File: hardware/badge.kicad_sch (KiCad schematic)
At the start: 2 parts

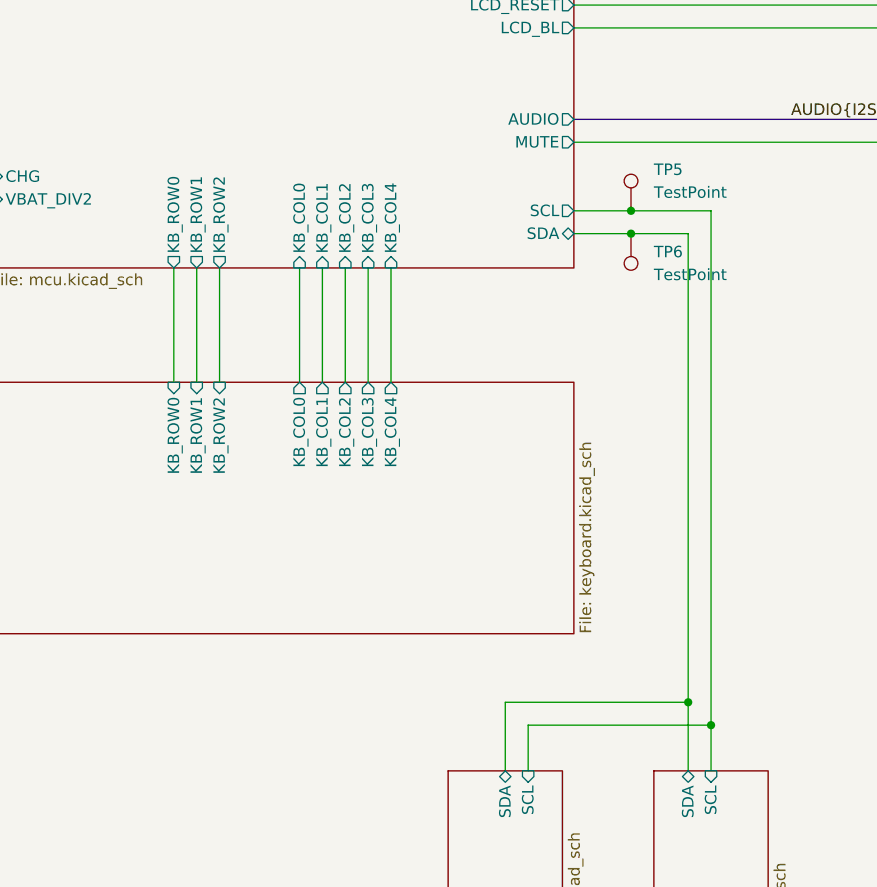
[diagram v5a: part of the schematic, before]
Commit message: remove mux, use i2c expander for keyboard
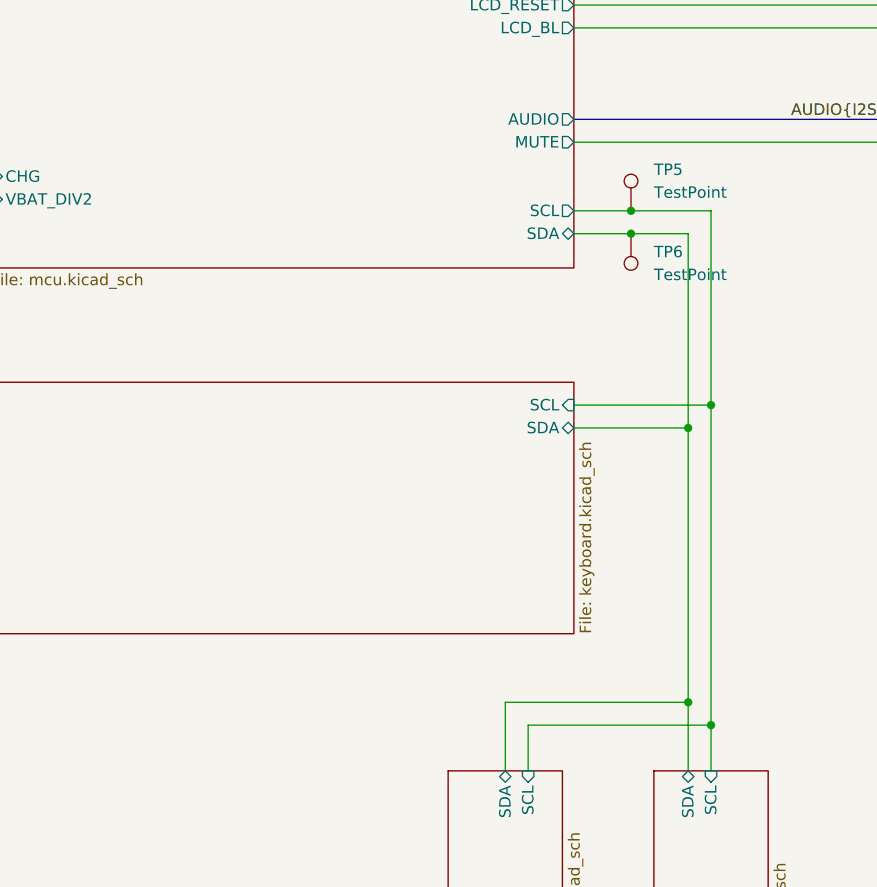
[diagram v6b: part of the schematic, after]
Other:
- sheet keyboard ports: added SCL, SDA; removed KB_COL0, KB_COL1, KB_COL2, KB_COL3, KB_COL4, KB_ROW0, KB_ROW1, KB_ROW2
- sheet mcu ports: added none; removed KB_COL0, KB_COL1, KB_COL2, KB_COL3, KB_COL4, KB_ROW0, KB_ROW1, KB_ROW2
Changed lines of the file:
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@@
+	)
+	(junction
+		(at 146.05 91.44)
+		(diameter 0)
+		(color 0 0 0 0)
 	)
 	(junction
@@
 		(color 0 0 0 0)
 	)
+	(junction
+		(at 148.59 88.9)
+		(diameter 0)
+		(color 0 0 0 0)
+	)
 	(no_connect
 		(at 196.85 49.53)
@@
 	(wire
 		(pts
-			(xy 91.44 73.66) (xy 91.44 86.36)
-		)
-		(stroke
-			(width 0)
-			(type default)
-		)
-	)
-	(wire
-		(pts
-			(xy 93.98 73.66) (xy 93.98 86.36)
-		)
-		(stroke
-			(width 0)
-			(type default)
-		)
-	)
-	(wire
-		(pts
 			(xy 133.35 44.45) (xy 196.85 44.45)
 		)
@@
 		)
 	)
-	(wire
-		(pts
-			(xy 113.03 73.66) (xy 113.03 86.36)
-		)
-		(stroke
-			(width 0)
-			(type default)
-		)
-	)
 	(bus
 		(pts
@@
 	(wire
 		(pts
-			(xy 146.05 69.85) (xy 146.05 121.92)
+			(xy 146.05 69.85) (xy 146.05 91.44)
 		)
 		(stroke
@@
 	(wire
 		(pts
-			(xy 148.59 67.31) (xy 148.59 124.46)
-		)
-		(stroke
-			(width 0)
-			(type default)
-		)
-	)
-	(wire
-		(pts
-			(xy 88.9 73.66) (xy 88.9 86.36)
+			(xy 148.59 67.31) (xy 148.59 88.9)
 		)
 		(stroke
@@
 		)
 	)
-	(wire
-		(pts
-			(xy 110.49 73.66) (xy 110.49 86.36)
-		)
-		(stroke
-			(width 0)
-			(type default)
-		)
-	)
 	(bus
 		(pts
@@
 	(wire
 		(pts
-			(xy 105.41 73.66) (xy 105.41 86.36)
-		)
-		(stroke
-			(width 0)
-			(type default)
-		)
-	)
-	(wire
-		(pts
 			(xy 58.42 36.83) (xy 68.58 36.83)
 		)
@@
 	(wire
 		(pts
+			(xy 146.05 91.44) (xy 146.05 121.92)
+		)
+		(stroke
+			(width 0)
+			(type default)
+		)
+	)
+	(wire
+		(pts
 			(xy 58.42 40.64) (xy 68.58 40.64)
 		)
@@
 	(wire
 		(pts
+			(xy 133.35 88.9) (xy 148.59 88.9)
+		)
+		(stroke
+			(width 0)
+			(type default)
+		)
+	)
+	(wire
+		(pts
 			(xy 139.7 67.31) (xy 148.59 67.31)
 		)
@@
 	(wire
 		(pts
-			(xy 107.95 73.66) (xy 107.95 86.36)
-		)
-		(stroke
-			(width 0)
-			(type default)
-		)
-	)
-	(wire
-		(pts
 			(xy 133.35 36.83) (xy 196.85 36.83)
 		)
@@
 	(wire
 		(pts
+			(xy 133.35 91.44) (xy 146.05 91.44)
+		)
+		(stroke
+			(width 0)
+			(type default)
+		)
+	)
+	(wire
+		(pts
 			(xy 148.59 124.46) (xy 148.59 129.54)
 		)
@@
 	(wire
 		(pts
-			(xy 102.87 73.66) (xy 102.87 86.36)
-		)
-		(stroke
-			(width 0)
-			(type default)
-		)
-	)
-	(wire
-		(pts
 			(xy 133.35 59.69) (xy 167.64 59.69)
+		)
+		(stroke
+			(width 0)
+			(type default)
+		)
+	)
+	(wire
+		(pts
+			(xy 148.59 88.9) (xy 148.59 124.46)
 		)
 		(stroke
@@
 			)
 		)
-		(pin "KB_ROW0" input
-			(at 88.9 86.36 90)
-			(effects
-				(font
-					(size 1.27 1.27)
-				)
-				(justify right)
-			)
-		)
-		(pin "KB_ROW1" input
-			(at 91.44 86.36 90)
-			(effects
-				(font
-					(size 1.27 1.27)
-				)
-				(justify right)
-			)
-		)
-		(pin "KB_ROW2" input
-			(at 93.98 86.36 90)
-			(effects
-				(font
-					(size 1.27 1.27)
-				)
-				(justify right)
-			)
-		)
-		(pin "KB_COL4" output
-			(at 113.03 86.36 90)
-			(effects
-				(font
-					(size 1.27 1.27)
-				)
-				(justify right)
-			)
-		)
-		(pin "KB_COL2" output
-			(at 107.95 86.36 90)
-			(effects
-				(font
-					(size 1.27 1.27)
-				)
-				(justify right)
-			)
-		)
-		(pin "KB_COL3" output
-			(at 110.49 86.36 90)
-			(effects
-				(font
-					(size 1.27 1.27)
-				)
-				(justify right)
-			)
-		)
-		(pin "KB_COL0" output
-			(at 102.87 86.36 90)
-			(effects
-				(font
-					(size 1.27 1.27)
-				)
-				(justify right)
-			)
-		)
-		(pin "KB_COL1" output
-			(at 105.41 86.36 90)
+		(pin "SCL" input
+			(at 133.35 88.9 0)
+			(effects
+				(font
+					(size 1.27 1.27)
+				)
+				(justify right)
+			)
+		)
+		(pin "SDA" bidirectional
+			(at 133.35 91.44 0)
 			(effects
 				(font
@@
 			)
 		)
-		(pin "KB_COL0" input
-			(at 102.87 73.66 270)
-			(effects
-				(font
-					(size 1.27 1.27)
-				)
-				(justify left)
-			)
-		)
-		(pin "KB_COL2" input
-			(at 107.95 73.66 270)
-			(effects
-				(font
-					(size 1.27 1.27)
-				)
-				(justify left)
-			)
-		)
-		(pin "KB_COL3" input
-			(at 110.49 73.66 270)
-			(effects
-				(font
-					(size 1.27 1.27)
-				)
-				(justify left)
-			)
-		)
-		(pin "KB_COL4" input
-			(at 113.03 73.66 270)
-			(effects
-				(font
-					(size 1.27 1.27)
-				)
-				(justify left)
-			)
-		)
-		(pin "KB_COL1" input
-			(at 105.41 73.66 270)
-			(effects
-				(font
-					(size 1.27 1.27)
-				)
-				(justify left)
-			)
-		)
 		(pin "CHG" input
 			(at 68.58 63.5 180)
@@
 			(effects
 				(font
-					(size 1.27 1.27)
-				)
-				(justify left)
-			)
-		)
-		(pin "KB_ROW0" output
-			(at 88.9 73.66 270)
-			(effects
-				(font
-					(size 1.27 1.27)
-				)
-				(justify left)
-			)
-		)
-		(pin "KB_ROW1" output
-			(at 91.44 73.66 270)
-			(effects
-				(font
-					(size 1.27 1.27)
-				)
-				(justify left)
-			)
-		)
-		(pin "KB_ROW2" output
-			(at 93.98 73.66 270)
-			(effects
-				(font

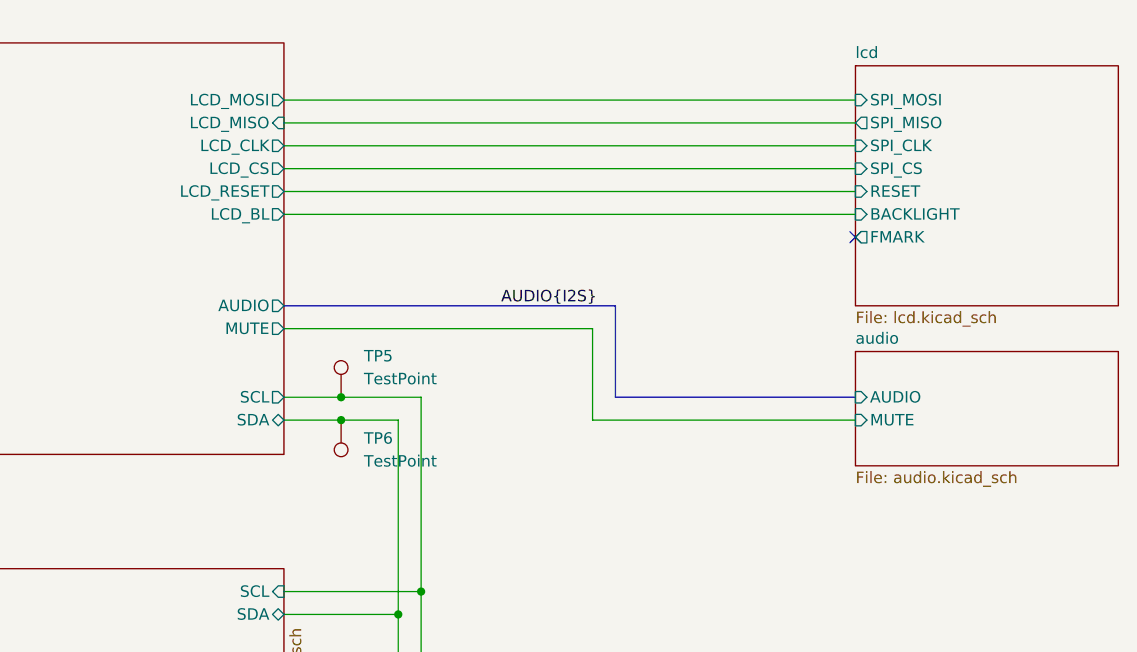
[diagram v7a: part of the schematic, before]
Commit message: Create a preliminary routing
Disconnect the LORA module from the lcd bus
Add netclass and lenght matching rule for the LCD signals
Use Bus for spi syglas for easy netclass association
Remove cutaway jumper for the io expansions, and hardcode the address
Routed the keyboard matrix
Change the LCD resistor to 1202
Fix the0Ohm resistor footprint
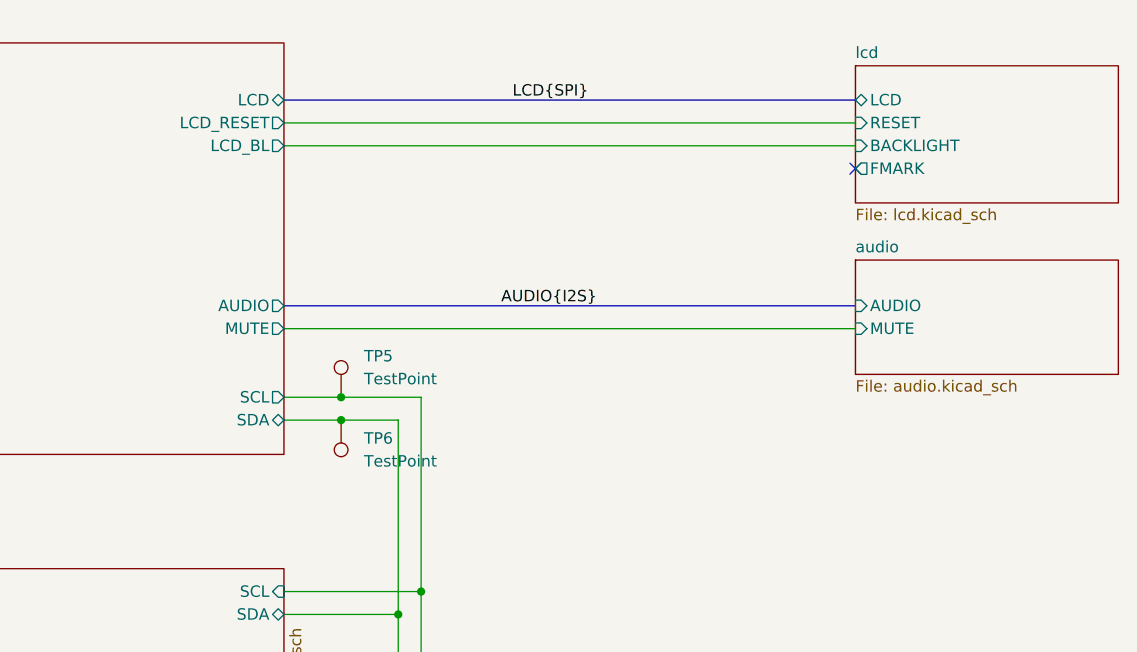
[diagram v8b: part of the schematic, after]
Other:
- sheet lcd ports: added LCD; removed SPI_CLK, SPI_CS, SPI_MISO, SPI_MOSI
- sheet mcu ports: added LCD; removed LCD_CLK, LCD_CS, LCD_MISO, LCD_MOSI
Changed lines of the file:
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@@
 	)
 	(no_connect
-		(at 196.85 49.53)
+		(at 196.85 41.91)
+	)
+	(wire
+		(pts
+			(xy 133.35 36.83) (xy 196.85 36.83)
+		)
+		(stroke
+			(width 0)
+			(type default)
+		)
+	)
+	(wire
+		(pts
+			(xy 146.05 121.92) (xy 146.05 129.54)
+		)
+		(stroke
+			(width 0)
+			(type default)
+		)
+	)
+	(bus
+		(pts
+			(xy 133.35 34.29) (xy 196.85 34.29)
+		)
+		(stroke
+			(width 0)
+			(type default)
+		)
 	)
 	(wire
@@
 		)
 	)
-	(wire
-		(pts
-			(xy 133.35 44.45) (xy 196.85 44.45)
-		)
-		(stroke
-			(width 0)
-			(type default)
-		)
-	)
-	(wire
-		(pts
-			(xy 133.35 34.29) (xy 196.85 34.29)
-		)
-		(stroke
-			(width 0)
-			(type default)
-		)
-	)
-	(wire
-		(pts
-			(xy 146.05 121.92) (xy 146.05 129.54)
-		)
-		(stroke
-			(width 0)
-			(type default)
-		)
-	)
 	(bus
 		(pts
-			(xy 133.35 57.15) (xy 170.18 57.15)
+			(xy 133.35 57.15) (xy 196.85 57.15)
 		)
 		(stroke
@@
 	(wire
 		(pts
-			(xy 133.35 41.91) (xy 196.85 41.91)
-		)
-		(stroke
-			(width 0)
-			(type default)
-		)
-	)
-	(wire
-		(pts
 			(xy 125.73 121.92) (xy 146.05 121.92)
 		)
@@
 		)
 	)
-	(bus
-		(pts
-			(xy 170.18 57.15) (xy 170.18 67.31)
-		)
-		(stroke
-			(width 0)
-			(type default)
-		)
-	)
-	(wire
-		(pts
-			(xy 196.85 69.85) (xy 167.64 69.85)
-		)
-		(stroke
-			(width 0)
-			(type default)
-		)
-	)
 	(wire
 		(pts
@@
 	(wire
 		(pts
-			(xy 133.35 46.99) (xy 196.85 46.99)
-		)
-		(stroke
-			(width 0)
-			(type default)
-		)
-	)
-	(wire
-		(pts
-			(xy 167.64 69.85) (xy 167.64 59.69)
-		)
-		(stroke
-			(width 0)
-			(type default)
-		)
-	)
-	(wire
-		(pts
 			(xy 128.27 124.46) (xy 148.59 124.46)
 		)
@@
 		)
 	)
-	(bus
-		(pts
-			(xy 170.18 67.31) (xy 196.85 67.31)
-		)
-		(stroke
-			(width 0)
-			(type default)
-		)
-	)
 	(wire
 		(pts
@@
 	(wire
 		(pts
-			(xy 133.35 36.83) (xy 196.85 36.83)
-		)
-		(stroke
-			(width 0)
-			(type default)
-		)
-	)
-	(wire
-		(pts
 			(xy 133.35 91.44) (xy 146.05 91.44)
 		)
@@
 	(wire
 		(pts
-			(xy 133.35 59.69) (xy 167.64 59.69)
+			(xy 133.35 59.69) (xy 196.85 59.69)
 		)
 		(stroke
@@
 		(at 157.48 57.15 0)
 		(fields_autoplaced yes)
+		(effects
+			(font
+				(size 1.27 1.27)
+			)
+			(justify left bottom)
+		)
+	)
+	(label "LCD{SPI}"
+		(at 158.75 34.29 0)
 		(effects
 			(font
@@
 	)
 	(sheet
-		(at 196.85 62.23)
+		(at 196.85 52.07)
 		(size 29.21 12.7)
 		(fields_autoplaced yes)
@@
 		)
 		(property "Sheetname" "audio"
-			(at 196.85 61.5184 0)
+			(at 196.85 51.3584 0)
 			(effects
 				(font
@@
 		)
 		(property "Sheetfile" "audio.kicad_sch"
-			(at 196.85 75.5146 0)
+			(at 196.85 65.3546 0)
 			(effects
 				(font
@@
 		)
 		(pin "AUDIO" input
-			(at 196.85 67.31 180)
+			(at 196.85 57.15 180)
 			(effects
 				(font
@@
 		)
 		(pin "MUTE" input
-			(at 196.85 69.85 180)
+			(at 196.85 59.69 180)
 			(effects
 				(font
@@
 	(sheet
 		(at 196.85 30.48)
-		(size 29.21 26.67)
+		(size 29.21 15.24)
 		(fields_autoplaced yes)
 		(stroke
@@
 		)
 		(property "Sheetfile" "lcd.kicad_sch"
-			(at 196.85 57.7346 0)
+			(at 196.85 46.3046 0)
 			(effects
 				(font
@@
 		)
 		(pin "RESET" input
-			(at 196.85 44.45 180)
-			(effects
-				(font
-					(size 1.27 1.27)
-				)
-				(justify left)
-			)
-		)
-		(pin "SPI_MOSI" input
+			(at 196.85 36.83 180)
+			(effects
+				(font
+					(size 1.27 1.27)
+				)
+				(justify left)
+			)
+		)
+		(pin "BACKLIGHT" input
+			(at 196.85 39.37 180)
+			(effects
+				(font
+					(size 1.27 1.27)
+				)
+				(justify left)
+			)
+		)
+		(pin "FMARK" output
+			(at 196.85 41.91 180)
+			(effects
+				(font
+					(size 1.27 1.27)
+				)
+				(justify left)
+			)
+		)
+		(pin "LCD" bidirectional
 			(at 196.85 34.29 180)
-			(effects
-				(font
-					(size 1.27 1.27)
-				)
-				(justify left)
-			)
-		)
-		(pin "SPI_CLK" input
-			(at 196.85 39.37 180)
-			(effects
-				(font
-					(size 1.27 1.27)
-				)
-				(justify left)
-			)
-		)
-		(pin "SPI_CS" input
-			(at 196.85 41.91 180)
-			(effects
-				(font
-					(size 1.27 1.27)
-				)
-				(justify left)
-			)
-		)
-		(pin "BACKLIGHT" input
-			(at 196.85 46.99 180)
-			(effects
-				(font
-					(size 1.27 1.27)
-				)
-				(justify left)
-			)
-		)
-		(pin "FMARK" output
-			(at 196.85 49.53 180)
-			(effects
-				(font
-					(size 1.27 1.27)
-				)
-				(justify left)
-			)
-		)
-		(pin "SPI_MISO" output
-			(at 196.85 36.83 180)
 			(effects
 				(font
@@
 			)
 		)
-		(pin "LCD_MISO" input
+		(pin "LCD_RESET" output
 			(at 133.35 36.83 0)
 			(effects
@@
 			)
 		)
-		(pin "LCD_CLK" output
+		(pin "LCD_BL" output
 			(at 133.35 39.37 0)
-			(effects
-				(font
-					(size 1.27 1.27)
-				)
-				(justify right)
-			)
-		)
-		(pin "LCD_MOSI" output
-			(at 133.35 34.29 0)
-			(effects
-				(font
-					(size 1.27 1.27)
-				)
-				(justify right)
-			)
-		)
-		(pin "LCD_RESET" output
-			(at 133.35 44.45 0)
-			(effects
-				(font
-					(size 1.27 1.27)
-				)
-				(justify right)
-			)
-		)
-		(pin "LCD_BL" output
-			(at 133.35 46.99 0)
 			(effects
 				(font
@@
 			)
 		)
-		(pin "LCD_CS" output
-			(at 133.35 41.91 0)
-			(effects
-				(font
+		(pin "LCD" bidirectional
+			(at 133.35 34.29 0)
+			(effects
+				(font
